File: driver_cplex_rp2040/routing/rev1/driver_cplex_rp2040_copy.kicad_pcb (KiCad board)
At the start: 6 copper layers, 40.2 x 40.2 mm, 479 parts, among them J1 Conn_01x05, J2 Conn_01x05, J3 Conn_01x05, J4 Conn_01x05, J5 Conn_01x04, Q1 1xPNP and 1xNPN, Q10 1xPNP and 1xNPN, Q11 1xPNP and 1xNPN, Q12 1xPNP and 1xNPN, Q13 1xPNP and 1xNPN, Q14 1xPNP and 1xNPN, Q15 1xPNP and 1xNPN, Q16 1xPNP and 1xNPN, Q17 1xPNP and 1xNPN, Q18 1xPNP and 1xNPN, Q19 1xPNP and 1xNPN, Q2 1xPNP and 1xNPN, Q20 1xPNP and 1xNPN, Q21 1xPNP and 1xNPN, Q22 1xPNP and 1xNPN, Q23 1xPNP and 1xNPN, Q24 1xPNP and 1xNPN, Q25 1xPNP and 1xNPN, Q26 1xPNP and 1xNPN, Q27 1xPNP and 1xNPN, Q28 1xPNP and 1xNPN, Q29 1xPNP and 1xNPN, Q3 1xPNP and 1xNPN, Q30 1xPNP and 1xNPN, Q31 1xPNP and 1xNPN, Q32 1xPNP and 1xNPN, Q33 1xPNP and 1xNPN, Q34 1xPNP and 1xNPN, Q4 1xPNP and 1xNPN, Q5 1xPNP and 1xNPN, Q6 1xPNP and 1xNPN, Q7 1xPNP and 1xNPN, Q8 1xPNP and 1xNPN, Q9 1xPNP and 1xNPN, SW1 SW_Push, SW2 SW_Push, U1 AP2112K-3.3, U2 RP2040, U3 W25Q16JVUXIQ_TR, Y1 12MHz

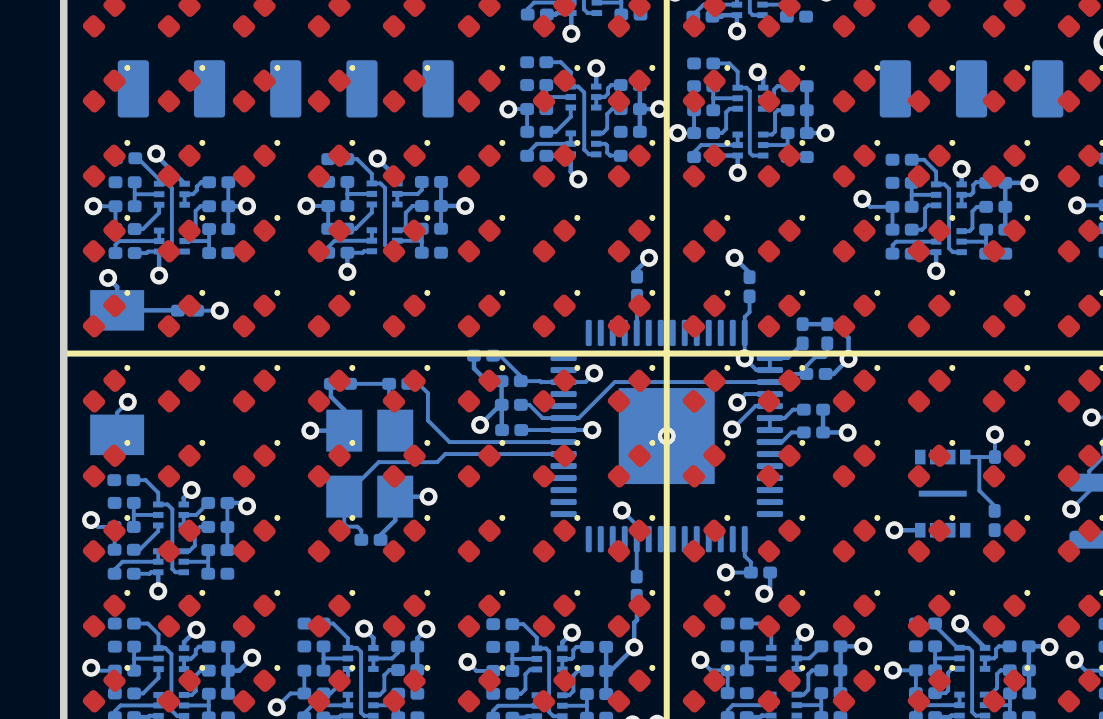
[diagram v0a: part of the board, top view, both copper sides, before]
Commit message: Worked on routing and layut for rp2040 cplex'd design.
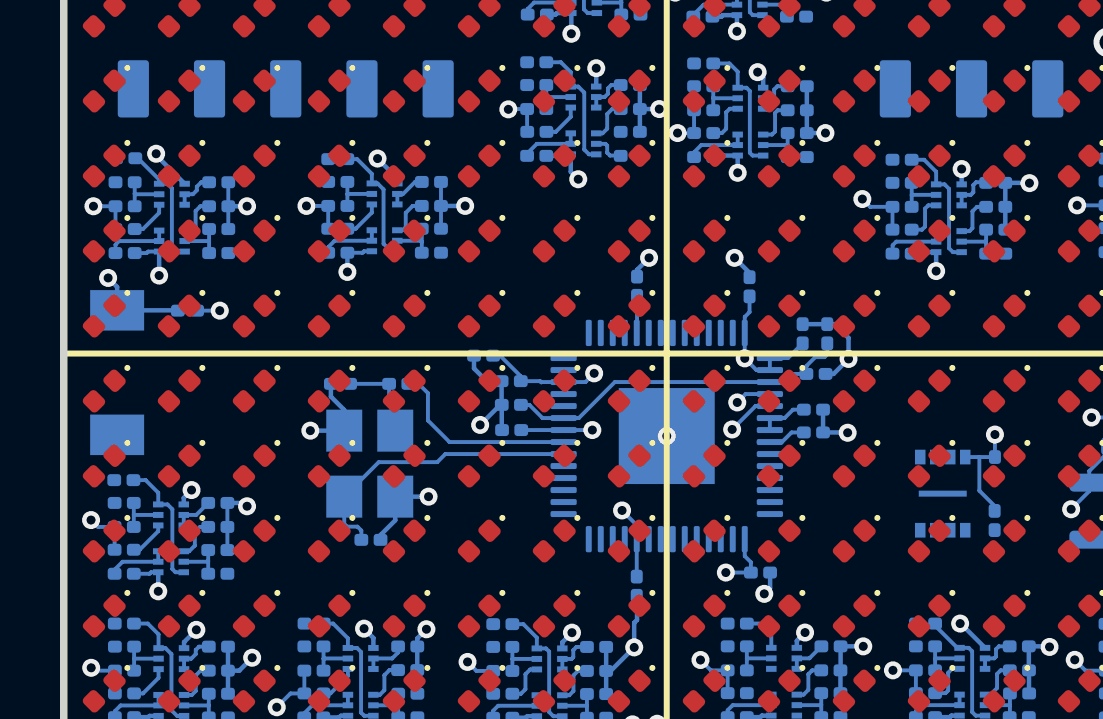
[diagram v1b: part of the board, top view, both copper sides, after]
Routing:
- net +3.3V: track 56.4 -> 55.2 mm, vias 27 -> 26
- net GND: track 87.1 -> 86.3 mm, vias 50 -> 49
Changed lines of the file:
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@@
   (layers
     (0 "F.Cu" signal)
-    (1 "In1.Cu" power)
-    (2 "In2.Cu" power)
+    (1 "In1.Cu" signal)
+    (2 "In2.Cu" signal)
     (3 "In3.Cu" signal)
-    (4 "In4.Cu" power)
+    (4 "In4.Cu" signal)
     (31 "B.Cu" signal)
     (34 "B.Paste" user)
@@
   (segment (start 58.565 79) (end 58.88 79) (width 0.13) (layer "B.Cu") (net 20))
   (segment (start 59.6774 79.8144) (end 59.3724 79.8144) (width 0.13) (layer "B.Cu") (net 20))
-  (segment (start 60.46 64.33) (end 60.61 64.48) (width 0.13) (layer "B.Cu") (net 21))
-  (segment (start 60.61 66.39) (end 60.81 66.59) (width 0.13) (layer "B.Cu") (net 21))
-  (segment (start 60.81 66.59) (end 61.02 66.59) (width 0.13) (layer "B.Cu") (net 21))
   (segment (start 60.17 64.01) (end 60.17 64.33) (width 0.13) (layer "B.Cu") (net 21))
+  (segment (start 60.36 64.33) (end 60.56 64.53) (width 0.13) (layer "B.Cu") (net 21))
   (segment (start 59.68 63.52) (end 60.17 64.01) (width 0.13) (layer "B.Cu") (net 21))
-  (segment (start 60.17 64.33) (end 60.46 64.33) (width 0.13) (layer "B.Cu") (net 21))
+  (segment (start 60.56 66.34) (end 60.81 66.59) (width 0.13) (layer "B.Cu") (net 21))
+  (segment (start 60.81 66.59) (end 61.02 66.59) (width 0.13) (layer "B.Cu") (net 21))
   (segment (start 59.355 63.52) (end 59.68 63.52) (width 0.13) (layer "B.Cu") (net 21))
-  (segment (start 60.61 64.48) (end 60.61 66.39) (width 0.13) (layer "B.Cu") (net 21))
+  (segment (start 60.56 64.53) (end 60.56 66.34) (width 0.13) (layer "B.Cu") (net 21))
+  (segment (start 60.17 64.33) (end 60.36 64.33) (width 0.13) (layer "B.Cu") (net 21))
   (segment (start 66.52 82.09) (end 66.22 82.09) (width 0.13) (layer "B.Cu") (net 22))
   (segment (start 65.975 79.83) (end 65.67 79.83) (width 0.13) (layer "B.Cu") (net 22))
@@
   (via (at 87.365 63.695) (size 0.6) (drill 0.3) (layers "F.Cu" "B.Cu") (net 34))
   (via (at 85.25 87.575) (size 1) (drill 0.6) (layers "F.Cu" "B.Cu") (net 34))
-  (via (at 77.590002 75.89) (size 0.6) (drill 0.3) (layers "F.Cu" "B.Cu") (net 34))
   (via (at 89.14 79.77) (size 0.6) (drill 0.3) (layers "F.Cu" "B.Cu") (net 34))
   (via (at 58.120002 72.57) (size 0.6) (drill 0.3) (layers "F.Cu" "B.Cu") (net 34))
@@
   (segment (start 53.93 64.34) (end 52.98 63.39) (width 0.15) (layer "B.Cu") (net 34))
   (segment (start 52.98 63.39) (end 52.98 63.34) (width 0.15) (layer "B.Cu") (net 34))
-  (segment (start 78.45 75.89) (end 77.590002 75.89) (width 0.15) (layer "B.Cu") (net 34))
   (segment (start 74.605 51.72) (end 74.605 52.52) (width 0.15) (layer "B.Cu") (net 34))
   (segment (start 69.105 61.85) (end 69.105 62.61) (width 0.15) (layer "B.Cu") (net 34))
@@
   (via (at 83.48 75.19) (size 0.6) (drill 0.3) (layers "F.Cu" "B.Cu") (net 35))
   (via (at 70.14 53.27) (size 0.6) (drill 0.3) (layers "F.Cu" "B.Cu") (net 35))
-  (via (at 52.034999 71.614999) (size 0.6) (drill 0.3) (layers "F.Cu" "B.Cu") (net 35))
   (via (at 64.72 61.86) (size 0.6) (drill 0.3) (layers "F.Cu" "B.Cu") (net 35))
   (segment (start 74.04 70.15) (end 74.53 69.66) (width 0.13) (layer "B.Cu") (net 35))
@@
   (segment (start 65.78 70.92) (end 65.82 70.96) (width 0.13) (layer "B.Cu") (net 35))
   (segment (start 51.625 65.09) (end 51.625 65.85) (width 0.13) (layer "B.Cu") (net 35))
-  (segment (start 51.68 71.969998) (end 52.034999 71.614999) (width 0.13) (layer "B.Cu") (net 35))
   (segment (start 64.444999 70.07) (end 65.135 70.760001) (width 0.13) (layer "B.Cu") (net 35))
   (segment (start 84.76 73.24) (end 84.76 73.09) (width 0.13) (layer "B.Cu") (net 35))
@@
   (segment (start 80.93 75.08) (end 80.42 74.57) (width 0.13) (layer "B.Cu") (net 35))
   (segment (start 72.6 69.3125) (end 72.6 68.78) (width 0.13) (layer "B.Cu") (net 35))
-  (segment (start 51.68 72.71) (end 51.68 71.969998) (width 0.13) (layer "B.Cu") (net 35))
   (segment (start 73.4375 70.55) (end 72.99 70.55) (width 0.13) (layer "B.Cu") (net 35))
   (segment (start 57.92 81.33) (end 57.46 81.33) (width 0.13) (layer "B.Cu") (net 35))
@@
   (segment (start 61.2 65.89) (end 61.3 65.79) (width 0.13) (layer "B.Cu") (net 69))
   (segment (start 61.53 65.08) (end 61.835 65.08) (width 0.13) (layer "B.Cu") (net 69))
-  (segment (start 61.7 64.68) (end 61.835 64.545) (width 0.13) (layer "B.Cu") (net 70))
-  (segment (start 61.02 64.68) (end 61.7 64.68) (width 0.13) (layer "B.Cu") (net 70))
-  (segment (start 61.835 64.545) (end 61.835 64.28) (width 0.13) (layer "B.Cu") (net 70))
+  (segment (start 61.21 64.68) (end 61.61 64.28) (width 0.13) (layer "B.Cu") (net 70))
+  (segment (start 61.61 64.28) (end 61.835 64.28) (width 0.13) (layer "B.Cu") (net 70))
+  (segment (start 61.02 64.68) (end 61.21 64.68) (width 0.13) (layer "B.Cu") (net 70))
   (segment (start 61.02 64.68) (end 61.02 65.03) (width 0.13) (layer "B.Cu") (net 70))
   (segment (start 61.835 66.28) (end 61.835 66.64) (width 0.13) (layer "B.Cu") (net 71))
